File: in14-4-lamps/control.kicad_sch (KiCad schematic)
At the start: 20 parts, among them J2 Conn_01x02_Pin, J3 Conn_01x06_Pin, Q10 2N7002, U3 ESP32-WROOM-32D, U4 DS3231M, U5 74141

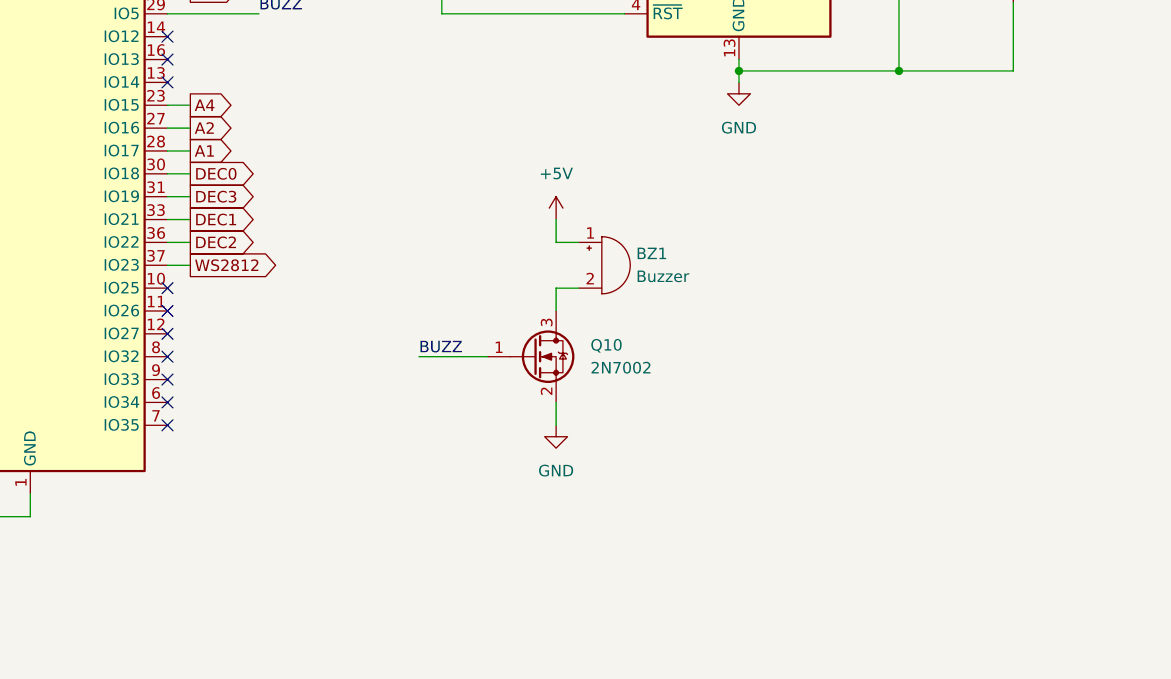
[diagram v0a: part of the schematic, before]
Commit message: add button and ws2812 connector
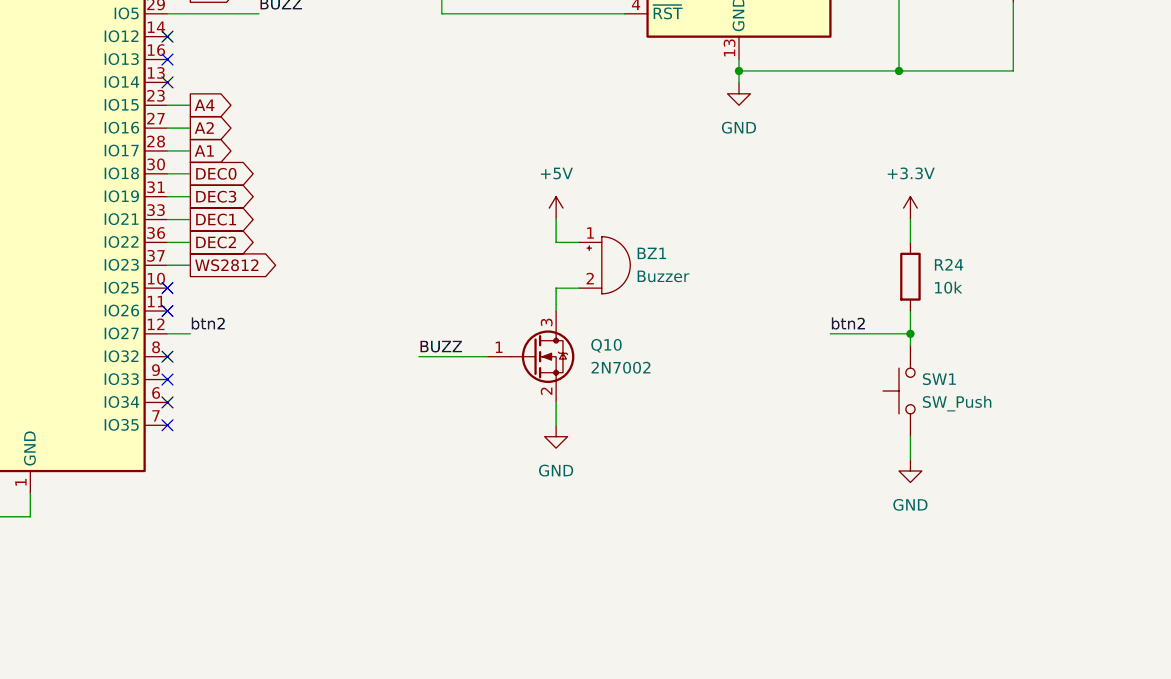
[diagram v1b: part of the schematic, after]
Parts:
- added R24: 10k, Resistor_SMD:R_0805_2012Metric_Pad1.20x1.40mm_HandSolder, symbol Device:R
- added SW1: SW_Push, Button_Switch_SMD:SW_Push_1P1T_NO_6x6mm_H9.5mm, symbol Switch:SW_Push
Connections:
- net +3.3V: now also R24.1
- net GND: now also SW1.1
- net btn2: now reaches U3.12 (IO27)
- net btn2: now also R24.2, SW1.2
- no-connect marks 18 -> 17
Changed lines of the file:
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@@
 (kicad_sch (version 20230121) (generator eeschema)
   (paper "A4")
+  (junction (at 161.29 91.44) (diameter 0) (color 0 0 0 0)
+  )
   (junction (at 139.7 30.48) (diameter 0) (color 0 0 0 0)
   )
@@
   (no_connect (at 48.26 81.28))
   (no_connect (at 78.74 101.6))
-  (no_connect (at 78.74 91.44))
   (no_connect (at 78.74 60.96))
   (no_connect (at 78.74 88.9))
@@
     (stroke (width 0) (type default))
   )
+  (wire (pts (xy 152.4 91.44) (xy 161.29 91.44))
+    (stroke (width 0) (type default))
+  )
   (wire (pts (xy 251.46 60.96) (xy 254 60.96))
     (stroke (width 0) (type default))
@@
     (stroke (width 0) (type default))
   )
+  (wire (pts (xy 161.29 91.44) (xy 161.29 92.71))
+    (stroke (width 0) (type default))
+  )
   (wire (pts (xy 172.72 27.94) (xy 142.24 27.94))
     (stroke (width 0) (type default))
@@
     (stroke (width 0) (type default))
   )
+  (wire (pts (xy 161.29 102.87) (xy 161.29 105.41))
+    (stroke (width 0) (type default))
+  )
   (wire (pts (xy 88.9 40.64) (xy 88.9 43.18))
     (stroke (width 0) (type default))
@@
     (stroke (width 0) (type default))
   )
+  (wire (pts (xy 81.28 91.44) (xy 78.74 91.44))
+    (stroke (width 0) (type default))
+  )
+  (wire (pts (xy 161.29 88.9) (xy 161.29 91.44))
+    (stroke (width 0) (type default))
+  )
   (wire (pts (xy 63.5 111.76) (xy 50.8 111.76))
     (stroke (width 0) (type default))
@@
     (stroke (width 0) (type default))
   )
+  (wire (pts (xy 161.29 78.74) (xy 161.29 81.28))
+    (stroke (width 0) (type default))
+  )
   (wire (pts (xy 109.22 40.64) (xy 109.22 55.88))
     (stroke (width 0) (type default))
@@
     (effects (font (size 1.27 1.27)) (justify left bottom))
   )
+  (label "btn2" (at 81.28 91.44 0) (fields_autoplaced)
+    (effects (font (size 1.27 1.27)) (justify left bottom))
+  )
   (label "BUZZ" (at 88.9 55.88 0) (fields_autoplaced)
     (effects (font (size 1.27 1.27)) (justify left bottom))
@@
   )
   (label "RX" (at 97.79 50.8 0) (fields_autoplaced)
+    (effects (font (size 1.27 1.27)) (justify left bottom))
+  )
+  (label "btn2" (at 152.4 91.44 0) (fields_autoplaced)
     (effects (font (size 1.27 1.27)) (justify left bottom))
   )
@@
     )
   )
+  (symbol (lib_id "power:+3.3V") (at 161.29 78.74 0) (unit 1)
+    (in_bom yes) (on_board yes) (dnp no) (fields_autoplaced)
+    (property "Reference" "#PWR029" (at 161.29 82.55 0)
+      (effects (font (size 1.27 1.27)) hide)
+    )
+    (property "Value" "+3.3V" (at 161.29 73.66 0)
+      (effects (font (size 1.27 1.27)))
+    )
+    (property "Footprint" "" (at 161.29 78.74 0)
+      (effects (font (size 1.27 1.27)) hide)
+    )
+    (property "Datasheet" "" (at 161.29 78.74 0)
+      (effects (font (size 1.27 1.27)) hide)
+    )
+    (pin "1")
+    (instances
+      (project "nixie-clock-esp-32"
+        (path "/cd8918ee-e986-4b1b-bef5-f32ed2eef1b1/6a0f8bd2-47e1-46cc-b2ff-e288ea213239"
+          (reference "#PWR029") (unit 1)
+        )
+      )
+    )
+  )
   (symbol (lib_id "power:+5V") (at 121.92 78.74 0) (unit 1)
     (in_bom yes) (on_board yes) (dnp no) (fields_autoplaced)
@@
         (path "/cd8918ee-e986-4b1b-bef5-f32ed2eef1b1/6a0f8bd2-47e1-46cc-b2ff-e288ea213239"
           (reference "BZ1") (unit 1)
+        )
+      )
+    )
+  )
+  (symbol (lib_id "Device:R") (at 161.29 85.09 0) (unit 1)
+    (in_bom yes) (on_board yes) (dnp no) (fields_autoplaced)
+    (property "Reference" "R24" (at 163.83 83.82 0)
+      (effects (font (size 1.27 1.27)) (justify left))
+    )
+    (property "Value" "10k" (at 163.83 86.36 0)
+      (effects (font (size 1.27 1.27)) (justify left))
+    )
+    (property "Footprint" "Resistor_SMD:R_0805_2012Metric_Pad1.20x1.40mm_HandSolder" (at 159.512 85.09 90)
+      (effects (font (size 1.27 1.27)) hide)
+    )
+    (property "Datasheet" "~" (at 161.29 85.09 0)
+      (effects (font (size 1.27 1.27)) hide)
+    )
+    (pin "1")
+    (pin "2")
+    (instances
+      (project "nixie-clock-esp-32"
+        (path "/cd8918ee-e986-4b1b-bef5-f32ed2eef1b1/6a0f8bd2-47e1-46cc-b2ff-e288ea213239"
+          (reference "R24") (unit 1)
+        )
+      )
+    )
+  )
+  (symbol (lib_id "power:GND") (at 161.29 105.41 0) (unit 1)
+    (in_bom yes) (on_board yes) (dnp no) (fields_autoplaced)
+    (property "Reference" "#PWR034" (at 161.29 111.76 0)
+      (effects (font (size 1.27 1.27)) hide)
+    )
+    (property "Value" "GND" (at 161.29 110.49 0)
+      (effects (font (size 1.27 1.27)))
+    )
+    (property "Footprint" "" (at 161.29 105.41 0)
+      (effects (font (size 1.27 1.27)) hide)
+    )
+    (property "Datasheet" "" (at 161.29 105.41 0)
+      (effects (font (size 1.27 1.27)) hide)
+    )
+    (pin "1")
+    (instances
+      (project "nixie-clock-esp-32"
+        (path "/cd8918ee-e986-4b1b-bef5-f32ed2eef1b1/6a0f8bd2-47e1-46cc-b2ff-e288ea213239"
+          (reference "#PWR034") (unit 1)
         )
       )
@@
         )
       )
+    )
+  )
+  (symbol (lib_id "Switch:SW_Push") (at 161.29 97.79 90) (unit 1)
+    (in_bom yes) (on_board yes) (dnp no) (fields_autoplaced)
+    (property "Reference" "SW1" (at 162.56 96.52 90)
+      (effects (font (size 1.27 1.27)) (justify right))
+    )
+    (property "Value" "SW_Push" (at 162.56 99.06 90)
+      (effects (font (size 1.27 1.27)) (justify right))
+    )
+    (property "Footprint" "Button_Switch_SMD:SW_Push_1P1T_NO_6x6mm_H9.5mm" (at 156.21 97.79 0)
+      (effects (font (size 1.27 1.27)) hide)
+    )
+    (property "Datasheet" "~" (at 156.21 97.79 0)
+      (effects (font (size 1.27 1.27)) hide)
+    )
+    (pin "1")
+    (pin "2")
+    (instances
+      (project "nixie-clock-esp-32"
+        (path "/cd8918ee-e986-4b1b-bef5-f32ed2eef1b1/6a0f8bd2-47e1-46cc-b2ff-e288ea213239"
+          (reference "SW1") (unit 1)
+        )
+      )

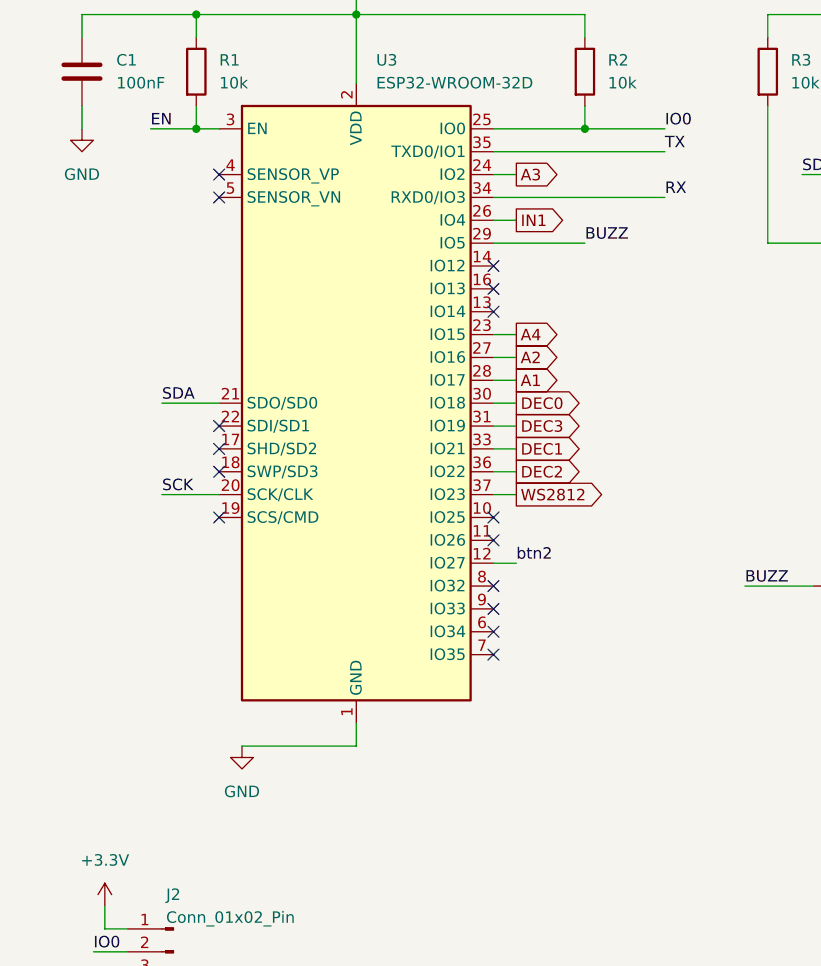
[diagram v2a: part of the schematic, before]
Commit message: fix i2c pins
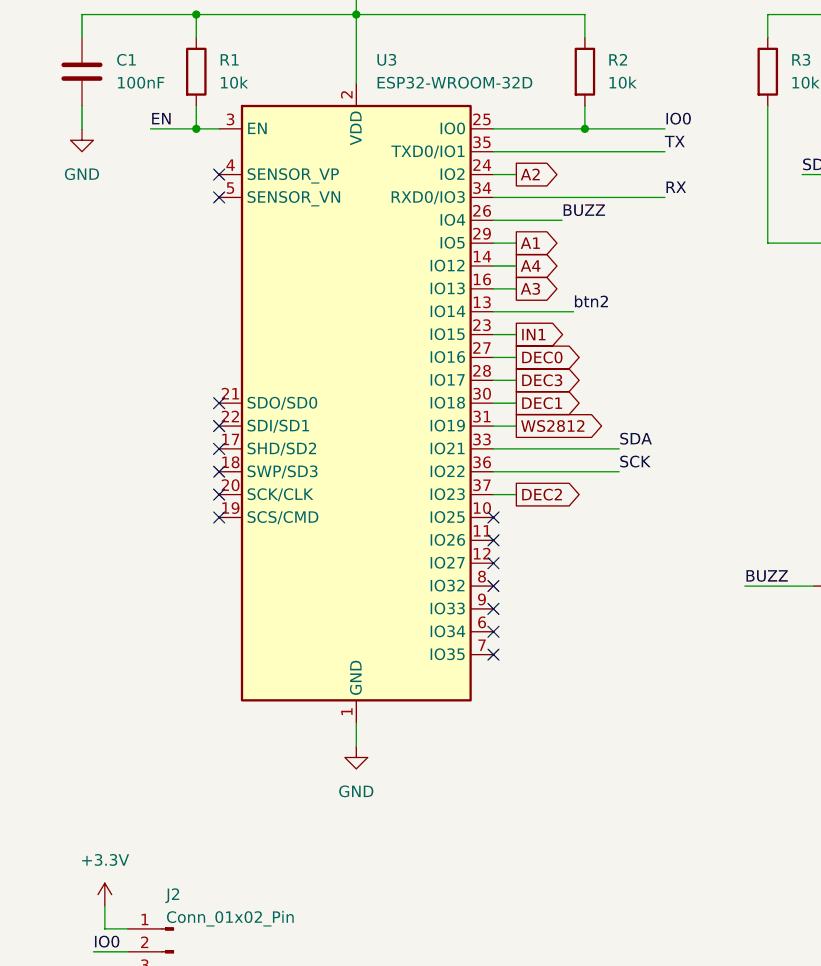
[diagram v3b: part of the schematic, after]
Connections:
- net A1: now also U3.29 (IO5); no longer U3.28 (IO17)
- net A2: now also U3.24 (IO2); no longer U3.27 (IO16)
- net A3: now also U3.16 (IO13); no longer U3.24 (IO2)
- net A4: now also U3.14 (IO12); no longer U3.23 (IO15)
- net BUZZ: now also U3.26 (IO4); no longer U3.29 (IO5)
- net DEC0: now also U3.27 (IO16); no longer U3.30 (IO18)
- net DEC1: now also U3.30 (IO18); no longer U3.33 (IO21)
- net DEC2: now also U3.37 (IO23); no longer U3.36 (IO22)
- net DEC3: now also U3.28 (IO17); no longer U3.31 (IO19)
- net IN1: now also U3.23 (IO15); no longer U3.26 (IO4)
- net SCK: now also U3.36 (IO22); no longer U3.20 (SCK/CLK)
- net SDA: now also U3.33 (IO21); no longer U3.21 (SDO/SD0)
- net WS2812: now also U3.31 (IO19); no longer U3.37 (IO23)
- net btn2: now also U3.13 (IO14); no longer U3.12 (IO27)
